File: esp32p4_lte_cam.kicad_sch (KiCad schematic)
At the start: 0 parts

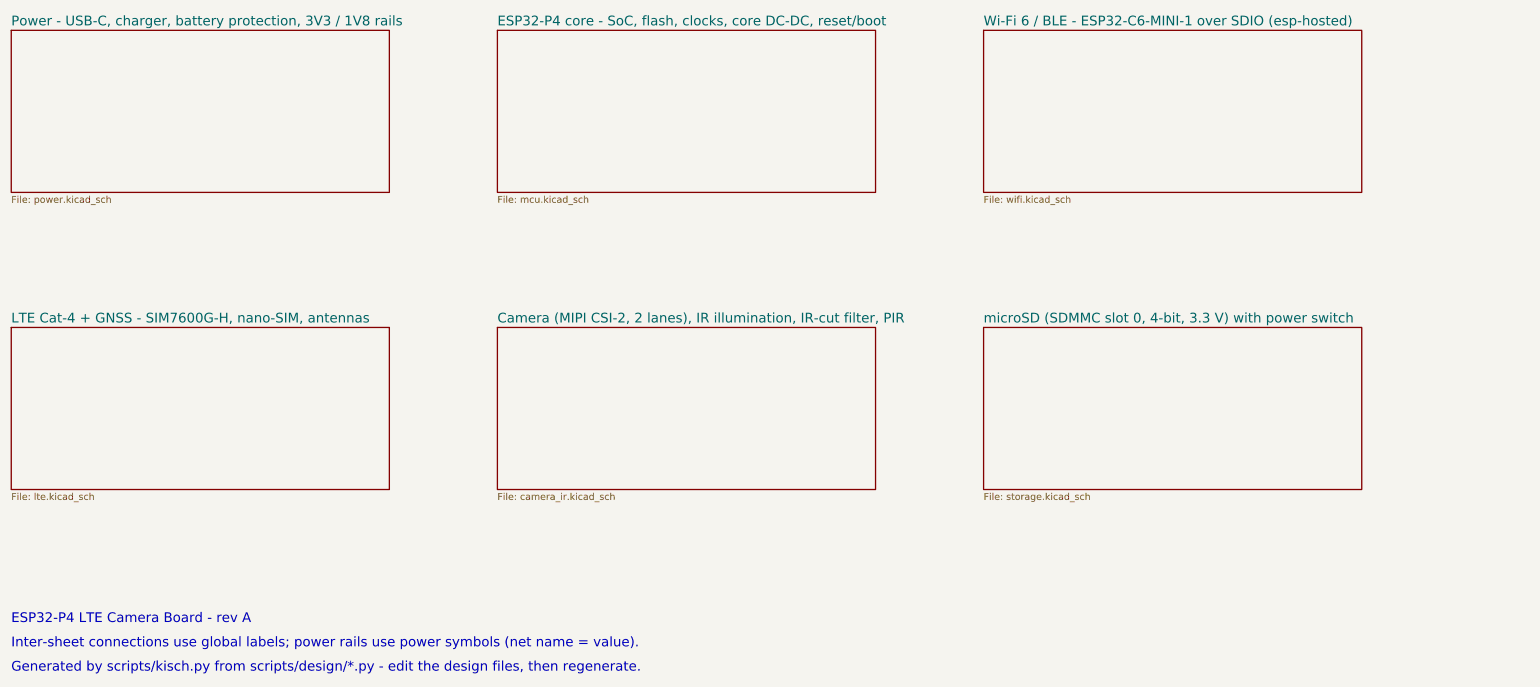
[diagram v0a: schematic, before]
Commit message: Phase 3: board setup
- Netlist -> PCB sync script (keeps placement, schematic links, LCSC/MPN fields)
- 75x70 mm outline, 4x M2.5 GND holes, JLC04161H-7628 stackup, L2 GND plane
- Net classes by pattern (Power, HighCurrent, RF 50R CPWG, USB 90R, MIPI 100R),
  JLC-checked rules and custom DRC rules; impedance calculator script
- Library fixes: peg holes -> NPTH, PIR courtyard, Espressif supply pin types
- Short sheet names so local nets read /power/..., /mcu/...
- DRC 0 violations; 231 footprints staged for placement

Co-Authored-By: Claude Opus 5.5 <noreply@anthropic.com>
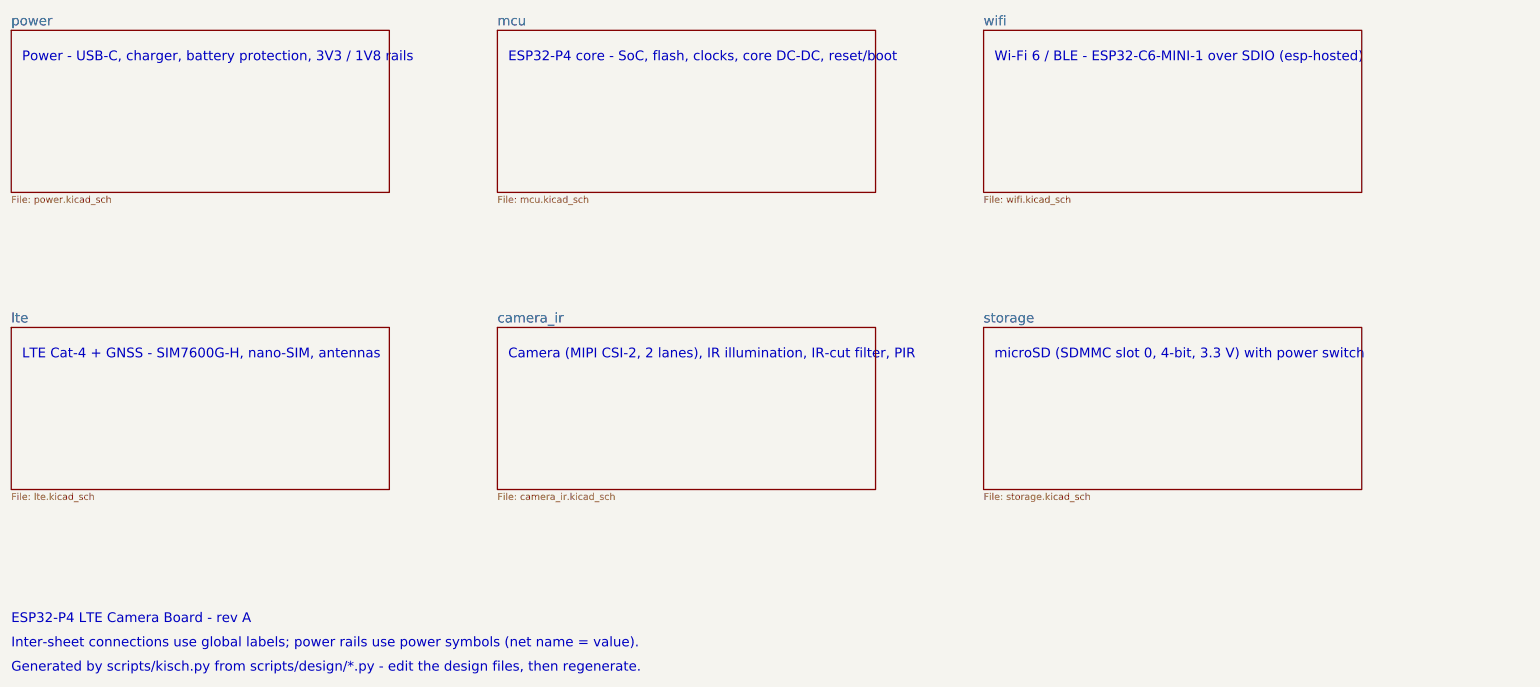
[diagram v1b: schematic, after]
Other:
- sheet Camera (MIPI CSI-2, 2 lanes), IR illumination, IR-cut filter, PIR renamed camera_ir
- sheet ESP32-P4 core - SoC, flash, clocks, core DC-DC, reset/boot renamed mcu
- sheet LTE Cat-4 + GNSS - SIM7600G-H, nano-SIM, antennas renamed lte
- sheet Power - USB-C, charger, battery protection, 3V3 / 1V8 rails renamed power
- sheet Wi-Fi 6 / BLE - ESP32-C6-MINI-1 over SDIO (esp-hosted) renamed wifi
- sheet microSD (SDMMC slot 0, 4-bit, 3.3 V) with power switch renamed storage
- note added: "Camera (MIPI CSI-2, 2 lanes), IR illumination, IR-cut filter, PIR"
- note added: "ESP32-P4 core - SoC, flash, clocks, core DC-DC, reset/boot"
- note added: "LTE Cat-4 + GNSS - SIM7600G-H, nano-SIM, antennas"
- note added: "Power - USB-C, charger, battery protection, 3V3 / 1V8 rails"
- note added: "Wi-Fi 6 / BLE - ESP32-C6-MINI-1 over SDIO (esp-hosted)"
- note added: "microSD (SDMMC slot 0, 4-bit, 3.3 V) with power switch"
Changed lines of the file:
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@@
 			(color 0 0 0 0)
 		)
-		(property "Sheetname" "Power - USB-C, charger, battery protection, 3V3 / 1V8 rails"
+		(property "Sheetname" "power"
 			(at 20 39.3 0)
 			(effects
@@
 		)
 	)
+	(text "Power - USB-C, charger, battery protection, 3V3 / 1V8 rails"
+		(exclude_from_sim no)
+		(at 22 46 0)
+		(effects
+			(font
+				(size 1.8 1.8)
+			)
+			(justify left bottom)
+		)
+	)
 	(sheet
 		(at 110 40)
@@
 			(color 0 0 0 0)
 		)
-		(property "Sheetname" "ESP32-P4 core - SoC, flash, clocks, core DC-DC, reset/boot"
+		(property "Sheetname" "mcu"
 			(at 110 39.3 0)
 			(effects
@@
 		)
 	)
+	(text "ESP32-P4 core - SoC, flash, clocks, core DC-DC, reset/boot"
+		(exclude_from_sim no)
+		(at 112 46 0)
+		(effects
+			(font
+				(size 1.8 1.8)
+			)
+			(justify left bottom)
+		)
+	)
 	(sheet
 		(at 200 40)
@@
 			(color 0 0 0 0)
 		)
-		(property "Sheetname" "Wi-Fi 6 / BLE - ESP32-C6-MINI-1 over SDIO (esp-hosted)"
+		(property "Sheetname" "wifi"
 			(at 200 39.3 0)
 			(effects
@@
 		)
 	)
+	(text "Wi-Fi 6 / BLE - ESP32-C6-MINI-1 over SDIO (esp-hosted)"
+		(exclude_from_sim no)
+		(at 202 46 0)
+		(effects
+			(font
+				(size 1.8 1.8)
+			)
+			(justify left bottom)
+		)
+	)
 	(sheet
 		(at 20 95)
@@
 			(color 0 0 0 0)
 		)
-		(property "Sheetname" "LTE Cat-4 + GNSS - SIM7600G-H, nano-SIM, antennas"
+		(property "Sheetname" "lte"
 			(at 20 94.3 0)
 			(effects
@@
 		)
 	)
+	(text "LTE Cat-4 + GNSS - SIM7600G-H, nano-SIM, antennas"
+		(exclude_from_sim no)
+		(at 22 101 0)
+		(effects
+			(font
+				(size 1.8 1.8)
+			)
+			(justify left bottom)
+		)
+	)
 	(sheet
 		(at 110 95)
@@
 			(color 0 0 0 0)
 		)
-		(property "Sheetname" "Camera (MIPI CSI-2, 2 lanes), IR illumination, IR-cut filter, PIR"
+		(property "Sheetname" "camera_ir"
 			(at 110 94.3 0)
 			(effects
@@
 		)
 	)
+	(text "Camera (MIPI CSI-2, 2 lanes), IR illumination, IR-cut filter, PIR"
+		(exclude_from_sim no)
+		(at 112 101 0)
+		(effects
+			(font
+				(size 1.8 1.8)
+			)
+			(justify left bottom)
+		)
+	)
 	(sheet
 		(at 200 95)
@@
 			(color 0 0 0 0)
 		)
-		(property "Sheetname" "microSD (SDMMC slot 0, 4-bit, 3.3 V) with power switch"
+		(property "Sheetname" "storage"
 			(at 200 94.3 0)
 			(effects
@@
 		)
 	)
+	(text "microSD (SDMMC slot 0, 4-bit, 3.3 V) with power switch"
+		(exclude_from_sim no)
+		(at 202 101 0)
+		(effects
+			(font
+				(size 1.8 1.8)
+			)
+			(justify left bottom)
+		)
+	)
